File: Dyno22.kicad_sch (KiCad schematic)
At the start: 28 parts, among them J1 Optical Sensor, J2 Pwr Input, J3 Force Sensor, J4 Brake Power Module, J5 I2C, U1 LM321

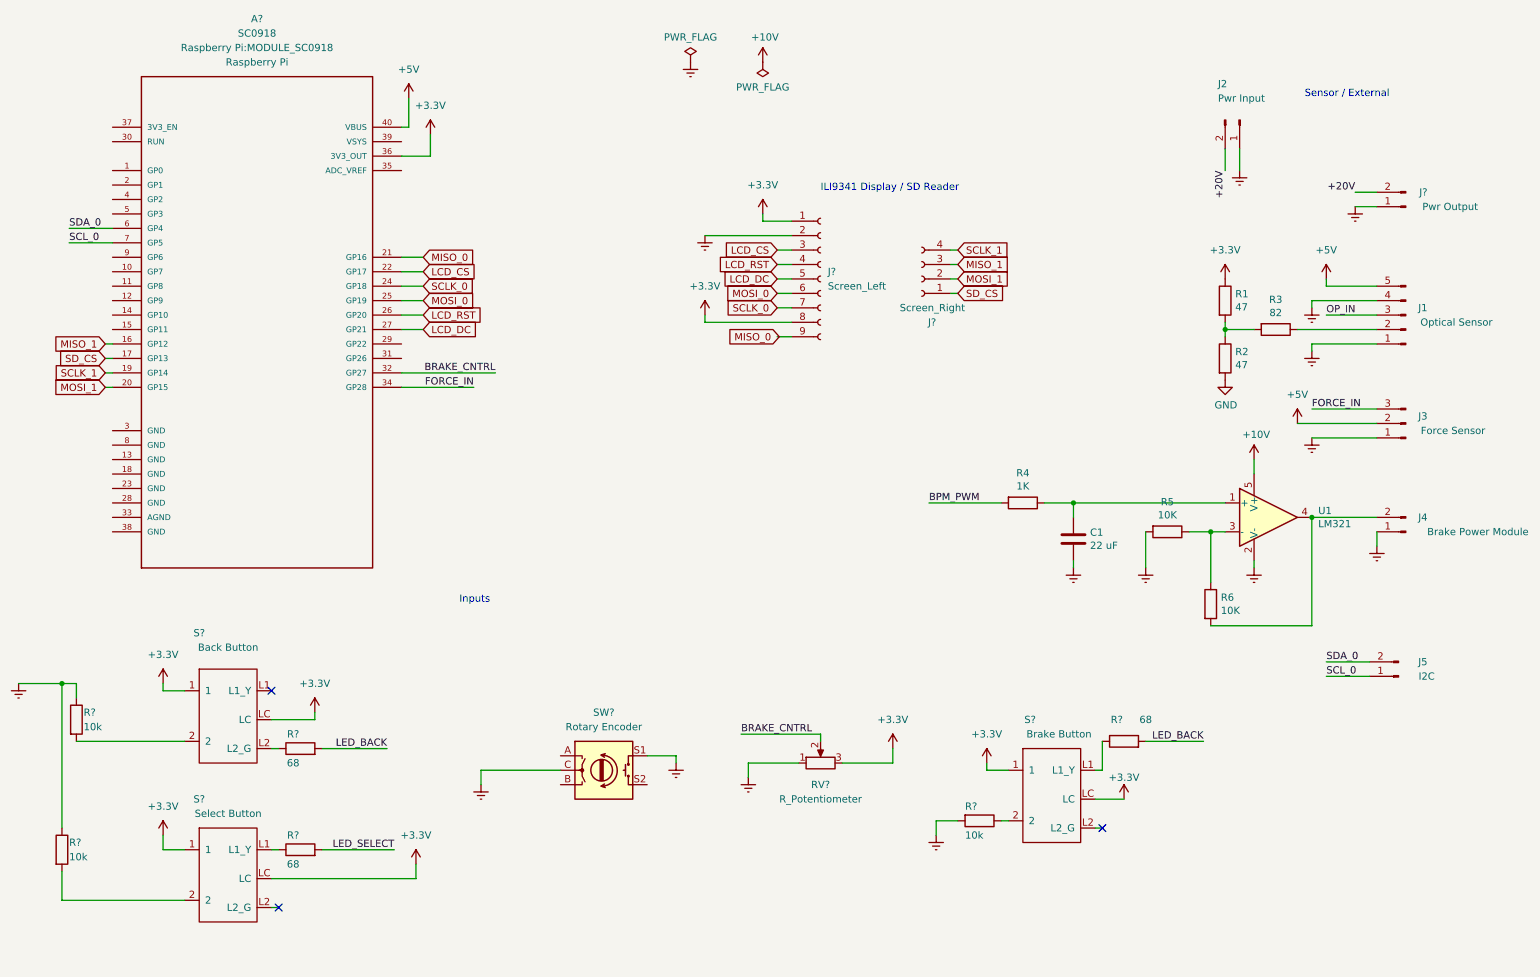
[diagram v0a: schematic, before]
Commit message: Fixes some labels--adds new label for 20V input
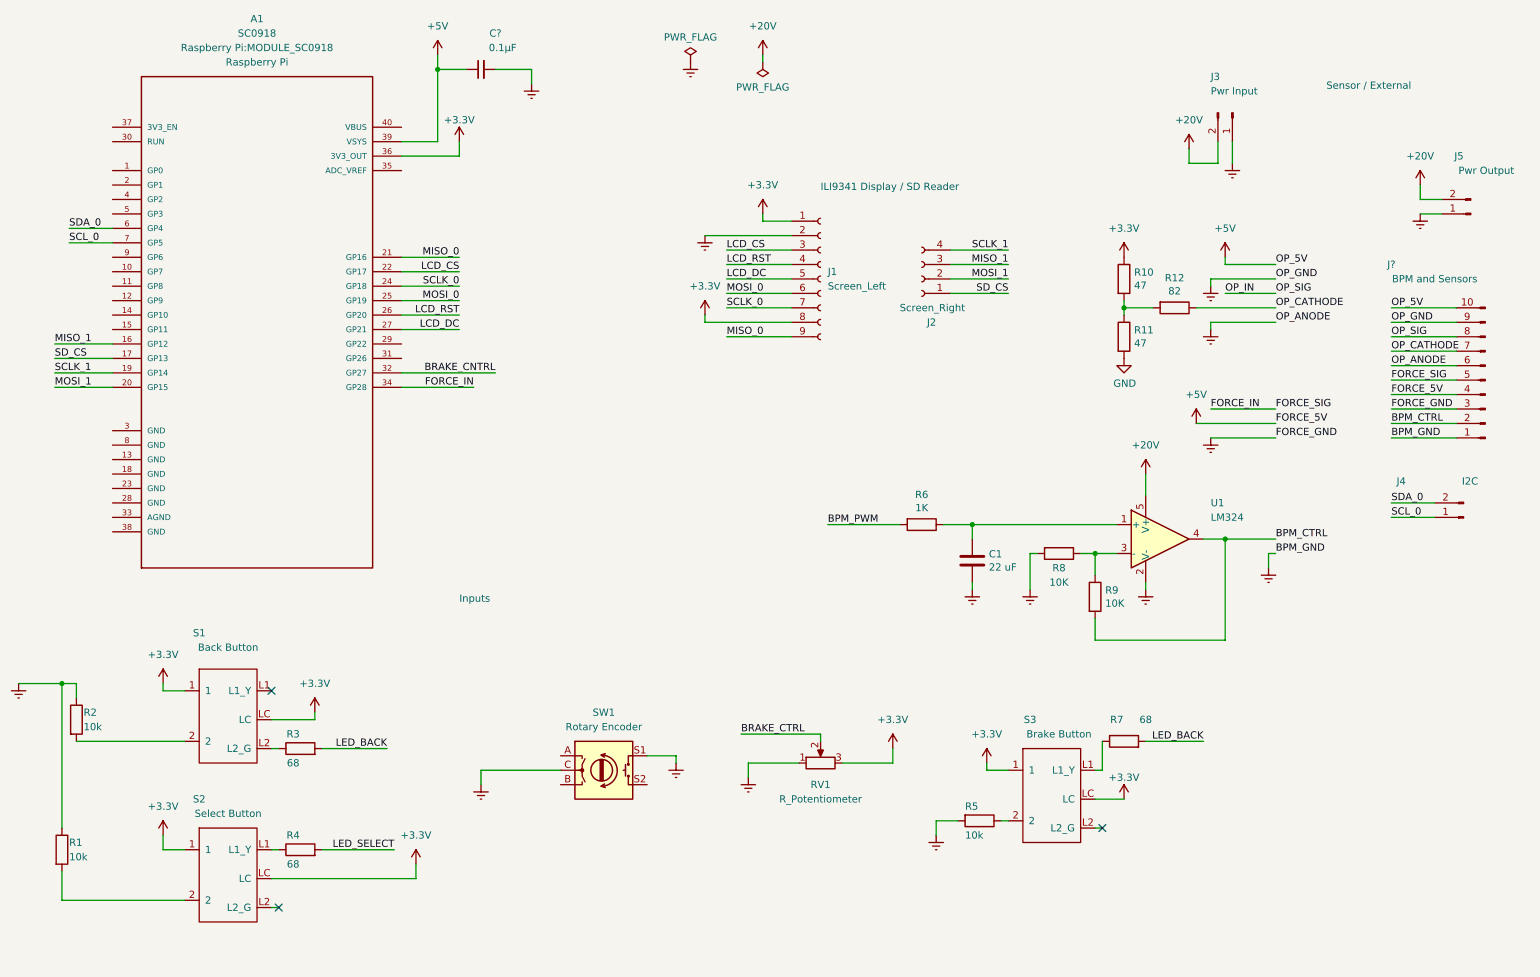
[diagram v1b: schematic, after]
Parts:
- removed J1: Optical Sensor, Connector_Molex:Molex_Nano-Fit_105310-xx06_2x03_P2.50mm_Vertical, symbol Connector:Conn_01x05_Male
- removed J3: Force Sensor, Connector_Molex:Molex_Nano-Fit_105314-xx04_2x02_P2.50mm_Horizontal, symbol Connector:Conn_01x03_Male
- removed J4: Brake Power Module, Connector_Molex:Molex_Nano-Fit_105313-xx02_1x02_P2.50mm_Horizontal, symbol Connector:Conn_01x02_Male
- added C?: 0.1µF, symbol Device:C_Small
- added J?: BPM and Sensors, symbol Connector:Conn_01x10_Male
- U1: value LM321 -> LM324
- gave numbers to parts that had none: 15
- renumbered J2 to J3, J5 to J4, R1 to R10, R2 to R11, R3 to R12, R4 to R6, R5 to R8, R6 to R9
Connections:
- net +20V is gone; now on net +24V: J3.2 (Pin_2), J5.2 (Pin_2)
- net +5V: now also A1.39 (VSYS), C?.1, J?.10 (Pin_10), J?.4 (Pin_4); no longer A1.40 (VBUS)
- net BRAKE_CNTRL: no longer RV1.2
- net Earth: now also C?.2, J?.1 (Pin_1), J?.3 (Pin_3), J?.6 (Pin_6), J?.9 (Pin_9)
- net FORCE_IN: now also J?.5 (Pin_5)
- net OP_IN: now also J?.8 (Pin_8)
- net OP_CATHODE: now reaches R12.1
- net OP_CATHODE: now also J?.7 (Pin_7)
- net BPM_CTRL: now reaches R9.2, U1.4
- net BPM_CTRL: now also J?.2 (Pin_2)
- net +10V renamed +24V
- new net BRAKE_CTRL: RV1.2
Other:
- moved on the sheet: C1, J3, J4, J5, R10, R11, R12, R6, R8, R9, U1

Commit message: Adds 5 -> 3.3V conversion for force and optical sensors
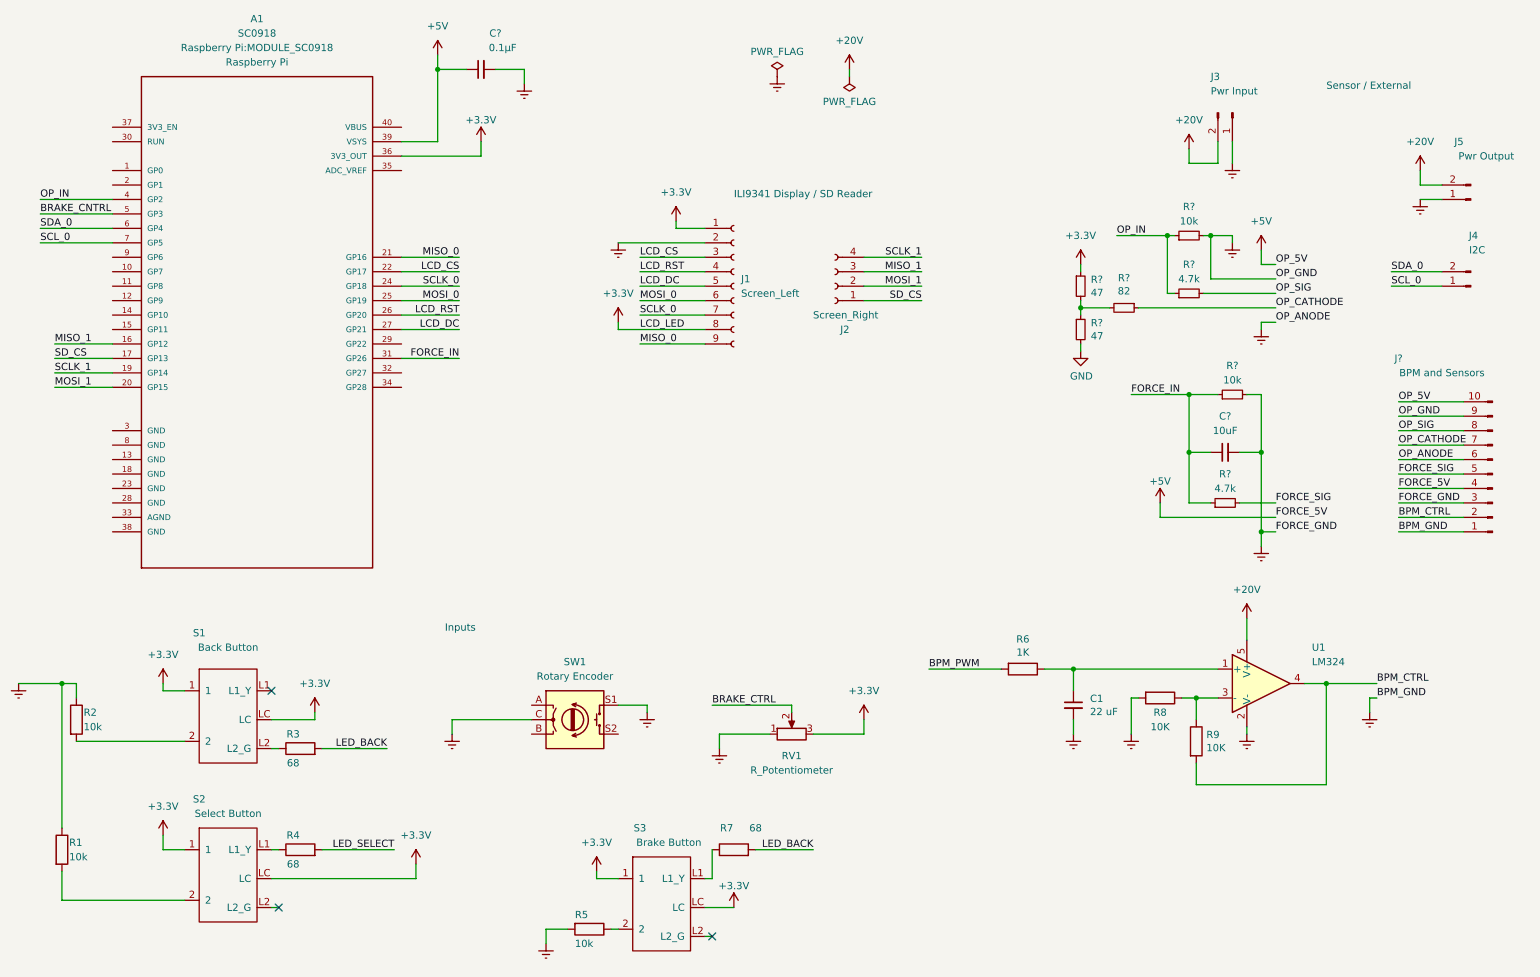
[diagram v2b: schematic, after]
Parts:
- removed R10, R11: 47, Resistor_SMD:R_0805_2012Metric_Pad1.20x1.40mm_HandSolder, symbol Device:R
- removed R12: 82, Resistor_SMD:R_0805_2012Metric_Pad1.20x1.40mm_HandSolder, symbol Device:R
- added C?: 10uF, symbol Device:C_Small
- added R? (x2): 4.7k, symbol Device:R_Small
- added R? (x2): 47, Resistor_SMD:R_0805_2012Metric_Pad1.20x1.40mm_HandSolder, symbol Device:R_Small
- added R?: 82, Resistor_SMD:R_0805_2012Metric_Pad1.20x1.40mm_HandSolder, symbol Device:R_Small
- added R? (x2): 10k, symbol Device:R_Small
- C1: symbol Device:C -> Device:C_Small
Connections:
- net +3.3V: now also R?.1
- net BRAKE_CNTRL: now also A1.5 (GP3); no longer A1.32 (GP27)
- net Earth: now also C?.2, R?.2, R?.2
- net FORCE_IN: now also A1.31 (GP26), C?.1, R?.1, R?.1; no longer A1.34 (GP28), J?.5 (Pin_5)
- net GND: now also R?.2
- net OP_CATHODE: now also R?.1
- net OP_IN: now also A1.4 (GP2), R?.1, R?.1; no longer J?.8 (Pin_8)
- new net: R?.1, R?.2, R?.2
- new net FORCE_SIG: J?.5 (Pin_5), R?.2
- new net OP_SIG: J?.8 (Pin_8), R?.2
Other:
- moved on the sheet: C1, J1, J2, J4, J5, J?, R5, R6, R7, R8, R9, RV1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

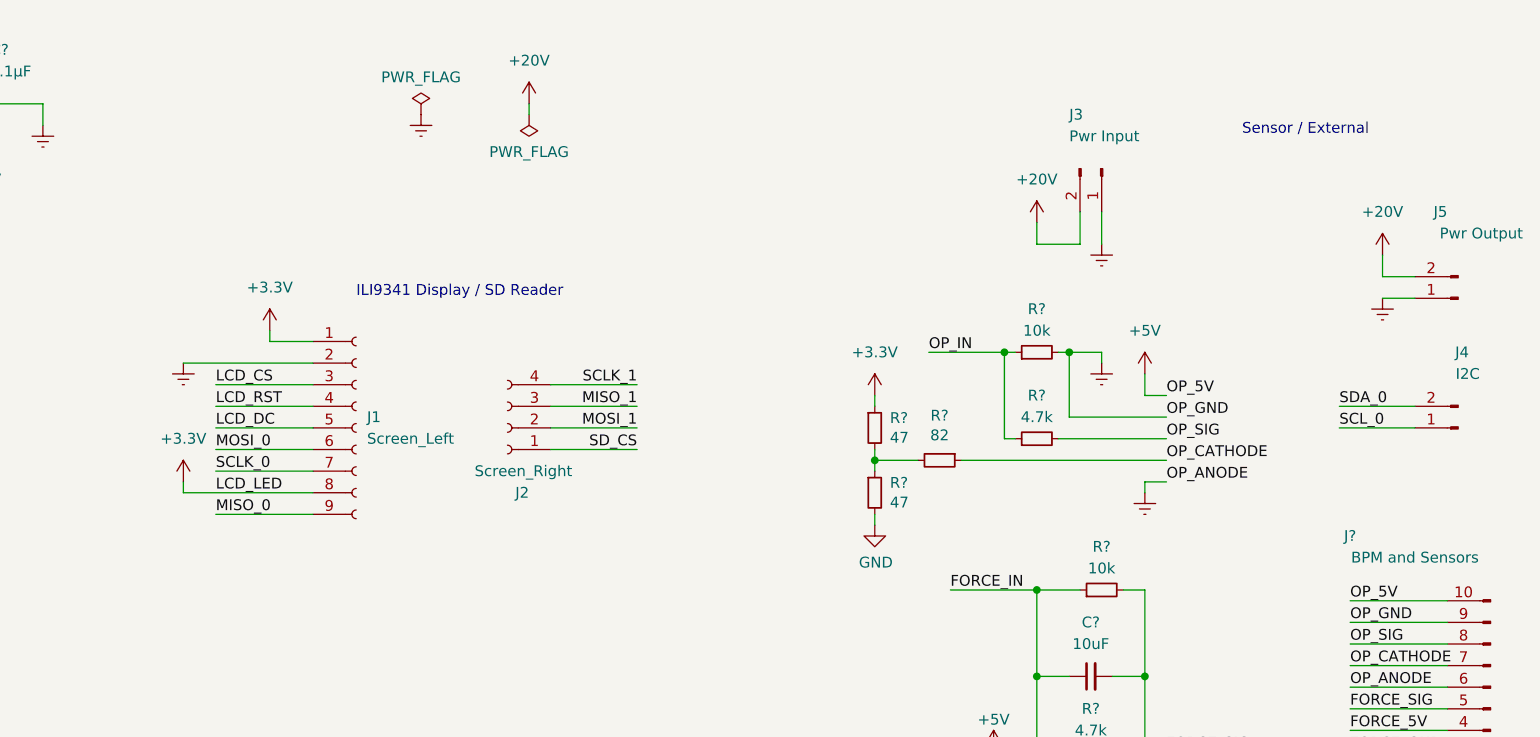
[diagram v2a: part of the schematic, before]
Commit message: Adds voltage regulator to power input
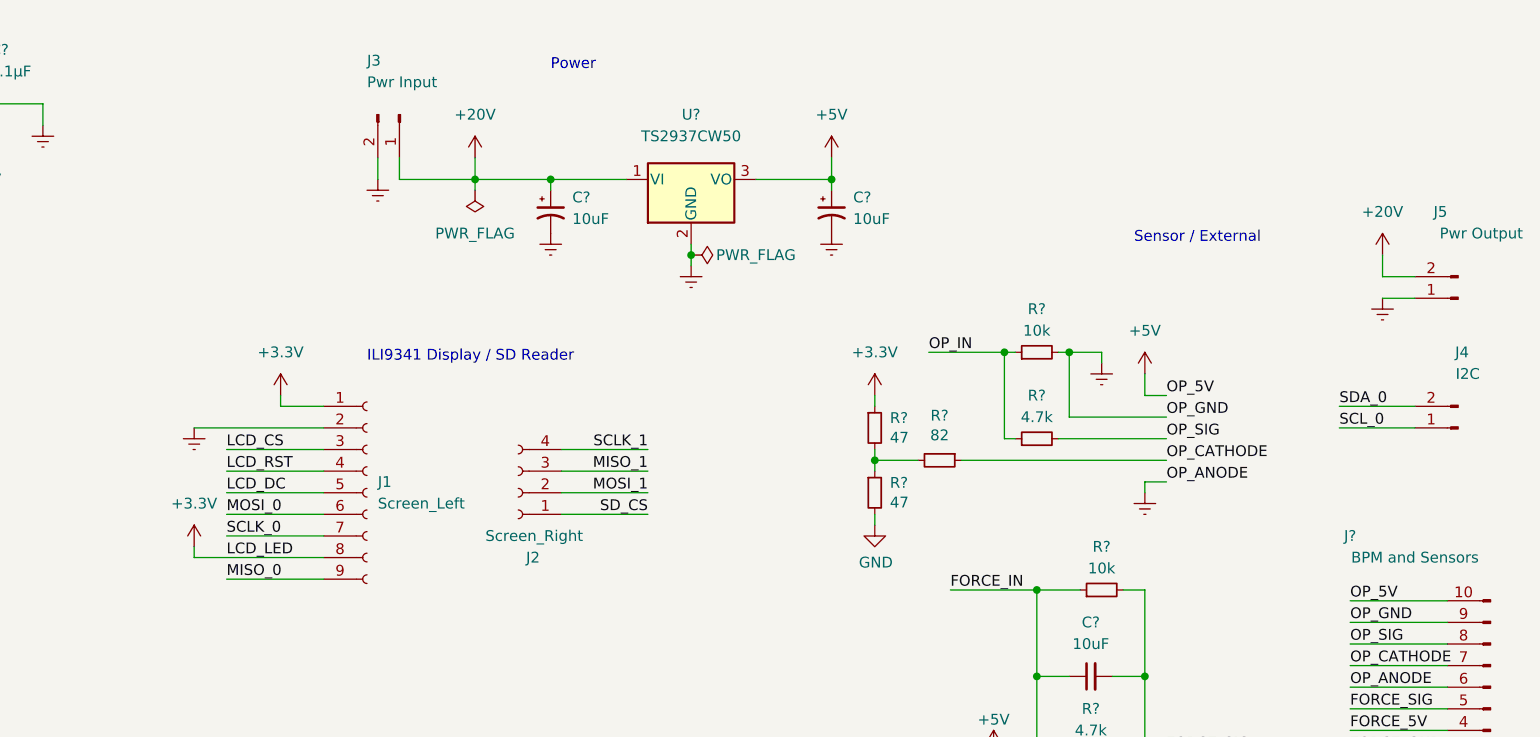
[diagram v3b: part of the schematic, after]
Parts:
- added C? (x2): 10uF, symbol Device:C_Polarized_Small_US
- added U?: TS2937CW50, Package_TO_SOT_SMD:SOT-223-3_TabPin2, symbol Regulator_Linear:LM2937xMP
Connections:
- net +24V: now also J3.1 (Pin_1), C?.1, U?.1 (VI); no longer J3.2 (Pin_2)
- net +5V: now also C?.1, U?.3 (VO)
- net Earth: now also J3.2 (Pin_2), C?.2, C?.2, U?.2 (GND); no longer J3.1 (Pin_1)
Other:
- note added: "Power"
- moved on the sheet: J1, J2, J3
